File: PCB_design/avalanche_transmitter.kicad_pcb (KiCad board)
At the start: 2 copper layers, 55 x 110 mm, 29 parts

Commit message: QOL additions
ready to print
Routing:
- net +3V0: track 170.4 -> 172.4 mm
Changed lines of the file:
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@@
   (segment (start 56.15 42.45) (end 55.935 42.235) (width 0.25) (layer "F.Cu") (net 2))
   (segment (start 47.8 40.9) (end 52.665 40.9) (width 0.25) (layer "F.Cu") (net 2))
-  (segment (start 61.1 26.302) (end 61.1 27.25) (width 0.25) (layer "F.Cu") (net 2))
   (segment (start 45.4 20.5) (end 46.3 19.6) (width 0.25) (layer "F.Cu") (net 2))
+  (segment (start 61 30.55) (end 61 28.2) (width 0.25) (layer "F.Cu") (net 2))
   (segment (start 41 41) (end 47.7 41) (width 0.25) (layer "F.Cu") (net 2))
   (segment (start 55.935 42.235) (end 54 42.235) (width 0.25) (layer "F.Cu") (net 2))
   (segment (start 52.665 40.9) (end 54 42.235) (width 0.25) (layer "F.Cu") (net 2))
+  (segment (start 57.15 24.35) (end 57.15 22.352) (width 0.25) (layer "F.Cu") (net 2))
   (segment (start 56.2 19.6) (end 57.15 20.55) (width 0.25) (layer "F.Cu") (net 2))
   (segment (start 56.01 37.85) (end 45.8 37.85) (width 0.25) (layer "F.Cu") (net 2))
-  (segment (start 57.15 22.352) (end 61.1 26.302) (width 0.25) (layer "F.Cu") (net 2))
   (segment (start 45.8 37.85) (end 45.4 37.45) (width 0.25) (layer "F.Cu") (net 2))
   (segment (start 59.05 40.89) (end 56.01 37.85) (width 0.25) (layer "F.Cu") (net 2))
+  (segment (start 61 28.2) (end 57.15 24.35) (width 0.25) (layer "F.Cu") (net 2))
   (segment (start 56.15 45.61) (end 56.15 42.45) (width 0.25) (layer "F.Cu") (net 2))
   (segment (start 46.3 19.6) (end 56.2 19.6) (width 0.25) (layer "F.Cu") (net 2))
   (segment (start 47.7 41) (end 47.8 40.9) (width 0.25) (layer "F.Cu") (net 2))
-  (via (at 61.1 27.25) (size 2.3) (drill 1.6) (layers "F.Cu" "B.Cu") (free) (net 2))
+  (via (at 61 30.55) (size 2.3) (drill 1.6) (layers "F.Cu" "B.Cu") (free) (net 2))
   (segment (start 78.2 80.1) (end 79.05 80.95) (width 0.25) (layer "B.Cu") (net 2))
-  (segment (start 82.25 49.175) (end 79.855 51.57) (width 0.25) (layer "B.Cu") (net 2))
-  (segment (start 66.15 32.2) (end 82.25 32.2) (width 0.25) (layer "B.Cu") (net 2))
   (segment (start 79.855 74.495) (end 78.2 76.15) (width 0.25) (layer "B.Cu") (net 2))
   (segment (start 79.855 51.57) (end 79.855 74.495) (width 0.25) (layer "B.Cu") (net 2))
-  (segment (start 82.25 32.2) (end 82.25 49.175) (width 0.25) (layer "B.Cu") (net 2))
   (segment (start 78.2 76.15) (end 78.2 80.1) (width 0.25) (layer "B.Cu") (net 2))
   (segment (start 79.05 93.06) (end 73.16 98.95) (width 0.25) (layer "B.Cu") (net 2))
   (segment (start 79.05 80.95) (end 79.05 93.06) (width 0.25) (layer "B.Cu") (net 2))
-  (segment (start 61.2 27.25) (end 66.15 32.2) (width 0.25) (layer "B.Cu") (net 2))
-  (segment (start 61.1 27.25) (end 61.2 27.25) (width 0.25) (layer "B.Cu") (net 2))
+  (segment (start 82.25 49.175) (end 79.855 51.57) (width 0.25) (layer "B.Cu") (net 2))
+  (segment (start 61 30.55) (end 62.65 32.2) (width 0.25) (layer "B.Cu") (net 2))
+  (segment (start 82.25 32.2) (end 82.25 49.175) (width 0.25) (layer "B.Cu") (net 2))
+  (segment (start 62.65 32.2) (end 82.25 32.2) (width 0.25) (layer "B.Cu") (net 2))
   (segment (start 62.16 20.62) (end 60.69 19.15) (width 0.25) (layer "F.Cu") (net 3))
   (segment (start 36.39 25.45) (end 36.39 83.99) (width 0.25) (layer "F.Cu") (net 3))
@@
   (segment (start 83.086396 83.1) (end 71.4 83.1) (width 0.25) (layer "F.Cu") (net 19))
   (segment (start 71.4 83.1) (end 70.58 82.28) (width 0.25) (layer "F.Cu") (net 19))
-  (segment (start 53.11 84.65) (end 53.21 84.75) (width 0.25) (layer "F.Cu") (net 20))
   (via (at 73.45 29.25) (size 2.3) (drill 1.6) (layers "F.Cu" "B.Cu") (free) (net 20))
-  (via (at 50.6 65.55) (size 2.3) (drill 1.6) (layers "F.Cu" "B.Cu") (free) (net 20))
+  (via (at 50.6 65.6) (size 2.3) (drill 1.6) (layers "F.Cu" "B.Cu") (free) (net 20))
   (via (at 41.1 27.5) (size 2.3) (drill 1.6) (layers "F.Cu" "B.Cu") (free) (net 20))
   (via (at 70.65 70.35) (size 2.3) (drill 1.6) (layers "F.Cu" "B.Cu") (free) (net 20))
-  (via (at 53.5 111.2) (size 2.3) (drill 1.6) (layers "F.Cu" "B.Cu") (free) (net 20))
-  (via (at 53.45 91.7) (size 2.3) (drill 1.6) (layers "F.Cu" "B.Cu") (free) (net 20))
-  (via (at 60.1 86.1) (size 2.3) (drill 1.6) (layers "F.Cu" "B.Cu") (free) (net 20))
+  (via (at 53.5 113.1) (size 2.3) (drill 1.6) (layers "F.Cu" "B.Cu") (free) (net 20))
+  (via (at 53.45 91.75) (size 2.3) (drill 1.6) (layers "F.Cu" "B.Cu") (free) (net 20))
+  (via (at 60.8 86.05) (size 2.3) (drill 1.6) (layers "F.Cu" "B.Cu") (free) (net 20))
   (segment (start 42.49 58.29) (end 45.45 58.29) (width 0.25) (layer "F.Cu") (net 21))
   (segment (start 47.64 56.1) (end 45.45 58.29) (width 0.25) (layer "F.Cu") (net 21))

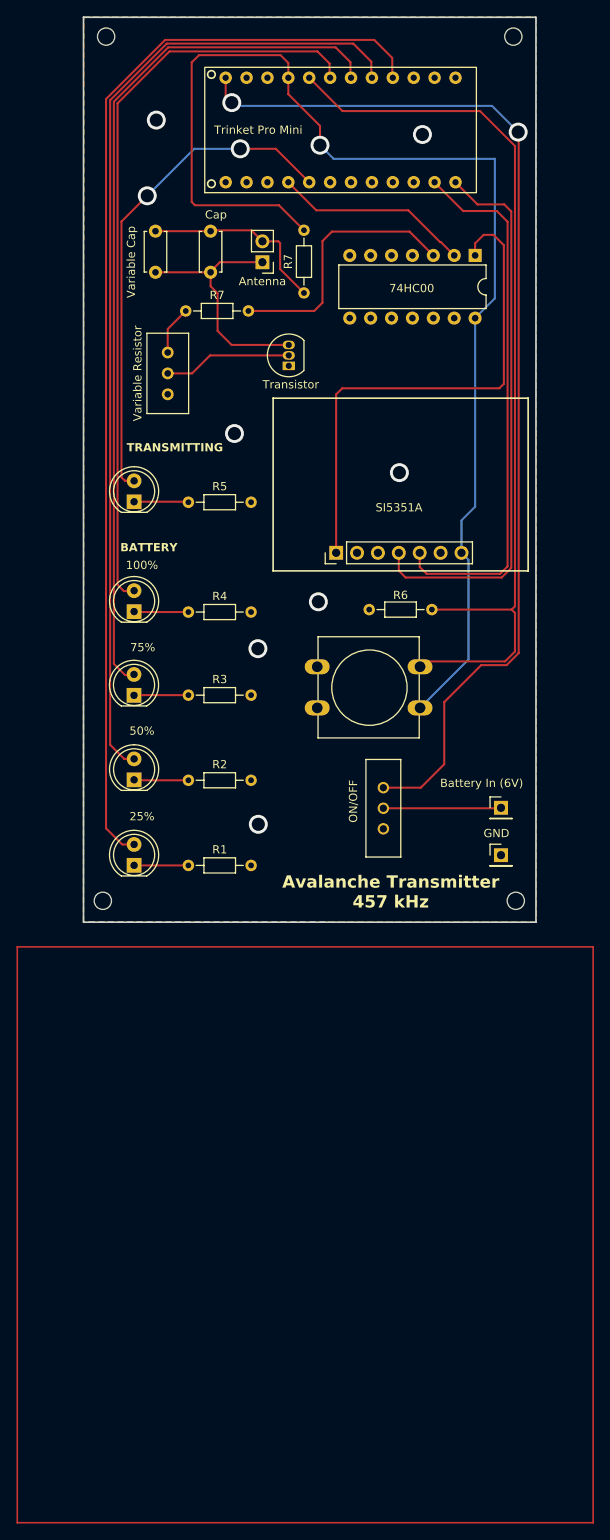
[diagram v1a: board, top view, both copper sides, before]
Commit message: Added voltage divider for battery check
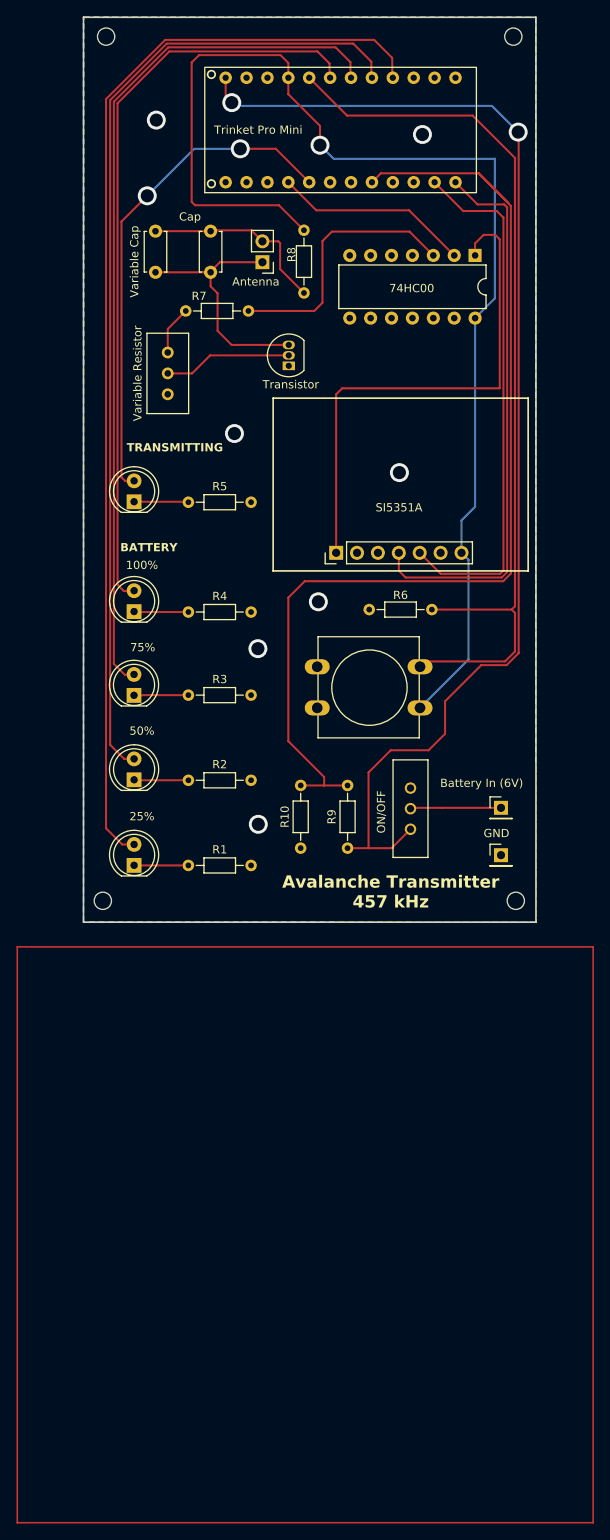
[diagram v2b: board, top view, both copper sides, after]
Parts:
- added R10: R_Small, Resistor_THT:R_Axial_DIN0204_L3.6mm_D1.6mm_P7.62mm_Horizontal, F.Cu at (58.6, 116.0)
- added R9: R_Small, Resistor_THT:R_Axial_DIN0204_L3.6mm_D1.6mm_P7.62mm_Horizontal, F.Cu at (64.3, 116.0)
- moved ON/OFF 6.03 mm to (72.0, 113.7), turned to 180 degrees
- renumbered R7 to R8
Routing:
- net unconnected-(U2-A1-Pad20): track 0.00 -> 127.5 mm
- net +6V: track 145.0 -> 158.6 mm
- net Net-(J1-Pin_5): track 66.0 -> 64.5 mm
- net Net-(U2-8): track 112.2 -> 111.4 mm

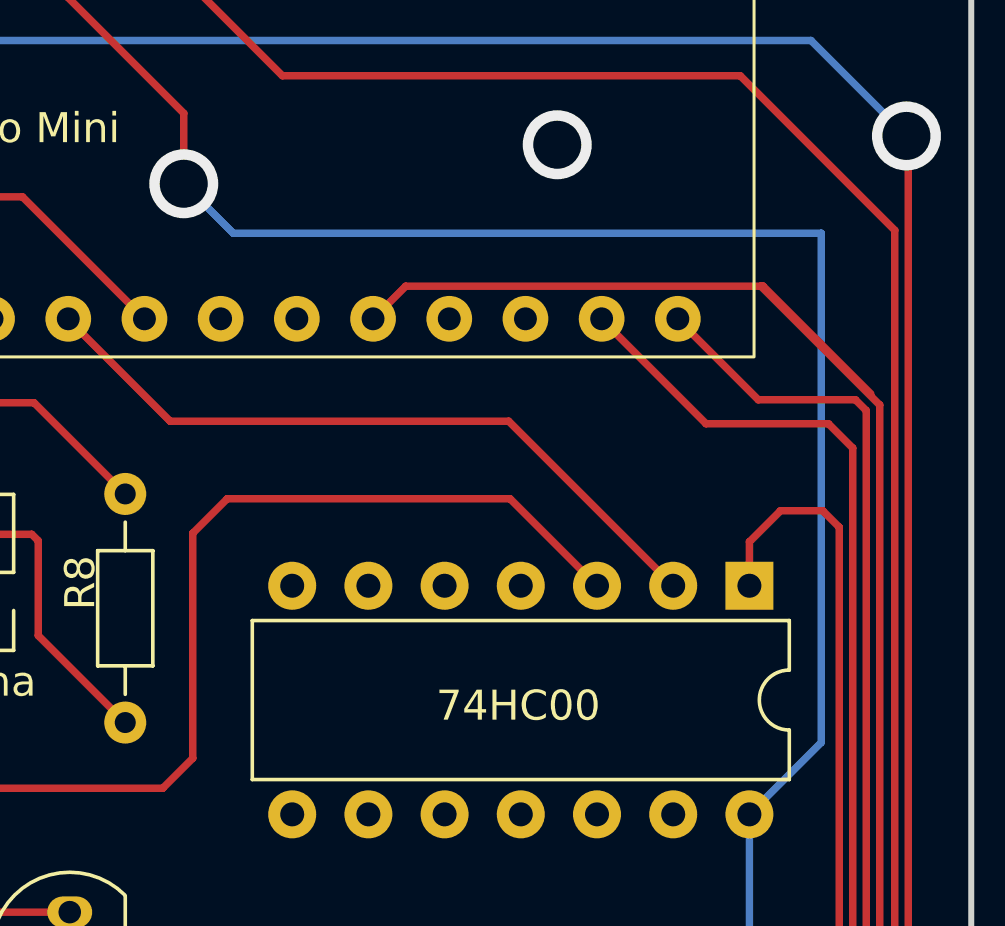
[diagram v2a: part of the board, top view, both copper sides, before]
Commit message: Manufacturing QOL updates
Moved some traces
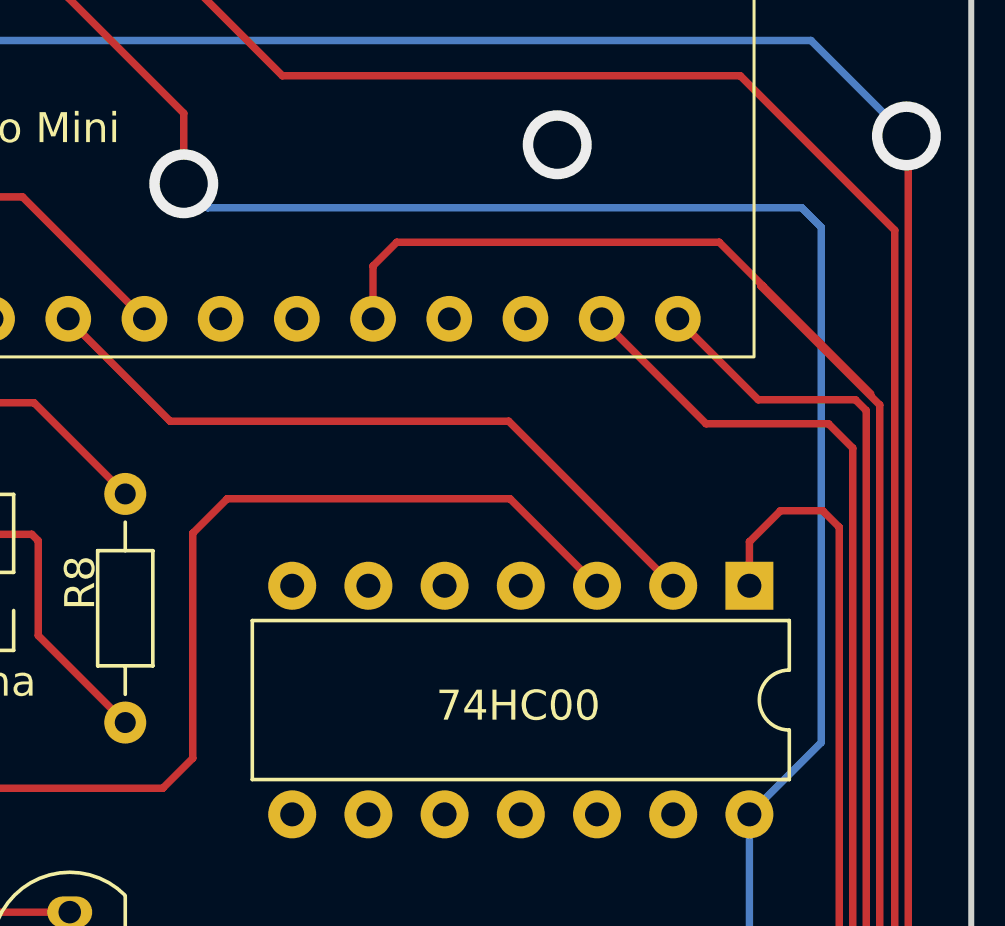
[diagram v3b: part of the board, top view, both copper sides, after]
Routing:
- net unconnected-(U2-A1-Pad20): track 127.5 -> 129.7 mm
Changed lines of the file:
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@@
   (via (at 61 30.55) (size 2.3) (drill 1.6) (layers "F.Cu" "B.Cu") (free) (net 2))
   (segment (start 78.2 80.1) (end 79.05 80.95) (width 0.25) (layer "B.Cu") (net 2))
+  (segment (start 61.8 31.35) (end 81.6 31.35) (width 0.25) (layer "B.Cu") (net 2))
+  (segment (start 82.25 49.175) (end 79.855 51.57) (width 0.25) (layer "B.Cu") (net 2))
   (segment (start 79.855 74.495) (end 78.2 76.15) (width 0.25) (layer "B.Cu") (net 2))
   (segment (start 79.855 51.57) (end 79.855 74.495) (width 0.25) (layer "B.Cu") (net 2))
   (segment (start 78.2 76.15) (end 78.2 80.1) (width 0.25) (layer "B.Cu") (net 2))
   (segment (start 79.05 93.06) (end 73.16 98.95) (width 0.25) (layer "B.Cu") (net 2))
+  (segment (start 82.25 32) (end 82.25 49.175) (width 0.25) (layer "B.Cu") (net 2))
   (segment (start 79.05 80.95) (end 79.05 93.06) (width 0.25) (layer "B.Cu") (net 2))
-  (segment (start 82.25 49.175) (end 79.855 51.57) (width 0.25) (layer "B.Cu") (net 2))
-  (segment (start 61 30.55) (end 62.65 32.2) (width 0.25) (layer "B.Cu") (net 2))
-  (segment (start 82.25 32.2) (end 82.25 49.175) (width 0.25) (layer "B.Cu") (net 2))
-  (segment (start 62.65 32.2) (end 82.25 32.2) (width 0.25) (layer "B.Cu") (net 2))
+  (segment (start 61 30.55) (end 61.8 31.35) (width 0.25) (layer "B.Cu") (net 2))
+  (segment (start 81.6 31.35) (end 82.25 32) (width 0.25) (layer "B.Cu") (net 2))
   (segment (start 62.16 20.62) (end 60.69 19.15) (width 0.25) (layer "F.Cu") (net 3))
   (segment (start 36.39 25.45) (end 36.39 83.99) (width 0.25) (layer "F.Cu") (net 3))
@@
   (segment (start 62.45 41.05) (end 71.875 41.05) (width 0.25) (layer "F.Cu") (net 24))
   (segment (start 71.875 41.05) (end 74.775 43.95) (width 0.25) (layer "F.Cu") (net 24))
+  (segment (start 68.1 32.5) (end 78.85 32.5) (width 0.25) (layer "F.Cu") (net 34))
   (segment (start 61.5 108.38) (end 58.65 108.38) (width 0.25) (layer "F.Cu") (net 34))
   (segment (start 59.15 83.55) (end 57.15 85.55) (width 0.25) (layer "F.Cu") (net 34))
   (segment (start 80.315 33.965) (end 80.241396 33.965) (width 0.25) (layer "F.Cu") (net 34))
   (segment (start 84.2 37.923604) (end 84.2 82.622792) (width 0.25) (layer "F.Cu") (net 34))
-  (segment (start 67.31 35.052) (end 68.397 33.965) (width 0.25) (layer "F.Cu") (net 34))
+  (segment (start 78.85 32.5) (end 80.315 33.965) (width 0.25) (layer "F.Cu") (net 34))
   (segment (start 83.272792 83.55) (end 59.15 83.55) (width 0.25) (layer "F.Cu") (net 34))
   (segment (start 80.315 33.965) (end 83.9 37.55) (width 0.25) (layer "F.Cu") (net 34))
-  (segment (start 68.397 33.965) (end 80.315 33.965) (width 0.25) (layer "F.Cu") (net 34))
   (segment (start 84.2 82.622792) (end 83.272792 83.55) (width 0.25) (layer "F.Cu") (net 34))
   (segment (start 61.5 107.35) (end 61.5 108.38) (width 0.25) (layer "F.Cu") (net 34))
+  (segment (start 67.31 35.052) (end 67.31 33.29) (width 0.25) (layer "F.Cu") (net 34))
   (segment (start 64.35 108.38) (end 61.5 108.38) (width 0.25) (layer "F.Cu") (net 34))
+  (segment (start 67.31 33.29) (end 68.1 32.5) (width 0.25) (layer "F.Cu") (net 34))
   (segment (start 57.15 103) (end 61.5 107.35) (width 0.25) (layer "F.Cu") (net 34))
   (segment (start 57.15 85.55) (end 57.15 103) (width 0.25) (layer "F.Cu") (net 34))

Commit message: Final PCB
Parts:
- removed 100%: RED_LED_100, LED_THT:LED_D5.0mm
- removed 25%: RED_LED_25, LED_THT:LED_D5.0mm
- removed 50%: RED_LED_50, LED_THT:LED_D5.0mm
- removed 74HC00: 74HC00, Package_DIP:DIP-14_W7.62mm
- removed 75%: RED_LED_75, LED_THT:LED_D5.0mm
- removed Antenna: Antenna_Loop, Connector_PinHeader_2.54mm:PinHeader_1x02_P2.54mm_Vertical
- removed Cap: C, Capacitor_THT:C_Disc_D4.7mm_W2.5mm_P5.00mm
- removed ON/OFF: SW_1218_EWI, SW_1218_EWI:SW_1218_EWI
- removed SI5351A: Conn_01x07_Pin, Connector_PinHeader_2.54mm:PinHeader_1x07_P2.54mm_Vertical
- removed TRANSMITTING: GREEN_LED, LED_THT:LED_D5.0mm
- removed Transistor: 2N3904, Package_TO_SOT_THT:TO-92_Inline
- removed Trinket Pro Mini: ~, ta:pro_mini
- removed Variable Cap: C_Variable, Capacitor_THT:C_Disc_D4.7mm_W2.5mm_P5.00mm
- removed Variable Resistor: R_Potentiometer, Potentiometer_THT:Potentiometer_Bourns_3296W_Vertical
- added 100%1: RED_LED_100, LED_THT:LED_D5.0mm, F.Cu at (38.4, 118.1)
- added 50%1: RED_LED_50, LED_THT:LED_D5.0mm, F.Cu at (38.4, 97.4)
- added 75%1: RED_LED_75, LED_THT:LED_D5.0mm, F.Cu at (38.4, 107.7)
- added AE1: Antenna_Loop, Connector_PinHeader_2.54mm:PinHeader_1x02_P2.54mm_Vertical, F.Cu at (54.0, 44.7)
- added C2: C_Variable, Capacitor_THT:C_Disc_D4.7mm_W2.5mm_P5.00mm, F.Cu at (41.0, 40.9)
- added C3: C, Capacitor_THT:C_Disc_D4.7mm_W2.5mm_P5.00mm, F.Cu at (47.8, 40.9)
- added D1: RED_LED_25, LED_THT:LED_D5.0mm, F.Cu at (38.4, 87.2)
- added J1: Conn_01x07_Pin, Connector_PinHeader_2.54mm:PinHeader_1x07_P2.54mm_Vertical, F.Cu at (63.0, 80.1)
- added Q1: 2N3904, Package_TO_SOT_THT:TO-92_Inline, F.Cu at (57.1, 57.3)
- added RV1: R_Potentiometer, Potentiometer_THT:Potentiometer_Bourns_3296W_Vertical, F.Cu at (42.5, 55.8)
- added SW2: SW_SPDT, Connector_PinHeader_2.54mm:PinHeader_1x03_P2.54mm_Vertical, F.Cu at (72.0, 113.8)
- added TRANSMITTING1: GREEN_LED, LED_THT:LED_D5.0mm, F.Cu at (38.4, 73.9)
- added U1: 74HC00, Package_DIP:DIP-14_W7.62mm, F.Cu at (79.9, 44.0)
- added U2: ~, ta:pro_mini, F.Cu at (63.5, 28.7)
- moved R1 30.9 mm to (45.0, 87.2)
- moved R4 30.8 mm to (45.0, 118.1)
- moved R2 10.3 mm to (45.0, 97.4)
- moved R3 10.3 mm to (45.0, 107.7)
- moved R9 7.67 mm to (64.4, 108.3), turned to -90 degrees
- moved R10 0.05 mm to (58.7, 116.0)
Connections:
- R10 pad 2: unconnected-(U2-A1-Pad20) -> Net-(U2-A1)
- R8 pad 1: +3V0 -> Net-(AE1-Pad2)
- R9 pad 1: +6V -> Net-(U2-A1)
- R9 pad 2: unconnected-(U2-A1-Pad20) -> /on/off
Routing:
- net +6V: track 158.6 -> 11.1 mm, vias 2 -> 0
- net /on/off: track 0.00 -> 146.1 mm, vias 0 -> 2
- net Net-(100%1-K): track 0.00 -> 135.6 mm
- net Net-(D4-K): track 133.9 -> 0.00 mm
- net unconnected-(U2-A1-Pad20): track 129.7 -> 0.00 mm
- net Net-(U2-A1): track 0.00 -> 124.6 mm
- net Net-(75%1-K): track 0.00 -> 121.3 mm
- net Net-(D3-K): track 119.5 -> 0.00 mm
- net Net-(50%1-K): track 0.00 -> 107.3 mm
- net Net-(D2-K): track 105.5 -> 0.00 mm
- net Net-(TRANSMITTING1-K): track 0.00 -> 62.7 mm, vias 0 -> 2
- net Net-(D5-K): track 60.4 -> 0.00 mm, vias 2 -> 0
- net Net-(AE1-Pad2): track 0.00 -> 23.1 mm
- net Net-(J1-Pin_1): track 62.6 -> 50.2 mm
- net +3V0: track 172.5 -> 178.3 mm, vias 1 -> 3
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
